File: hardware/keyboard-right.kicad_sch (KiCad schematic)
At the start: 84 parts, among them J1 BATT, J2 nice!view, J4 NUM_PAD, SW1 ON/OFF, SW10 U, SW11 I, SW12 O, SW13 P, SW14 {, SW15 H, SW16 J, SW17 K, SW18 L, SW19 ;, SW2 NRST, SW20 ', SW21 __ENTER, SW22 N, SW23 M, SW24 ,, SW25 ., SW26 /, SW27 SHIFT, SW28 UP, SW29 M1, SW3 6, SW30 DOWN, SW31 LEFT, SW32 ALT_2, SW33 RIGHT, SW34 DEL, SW35 }, SW36 SPACE, SW4 7, SW5 8, SW6 9, SW7 0, SW8 -, SW9 Y, U1 nice!nano

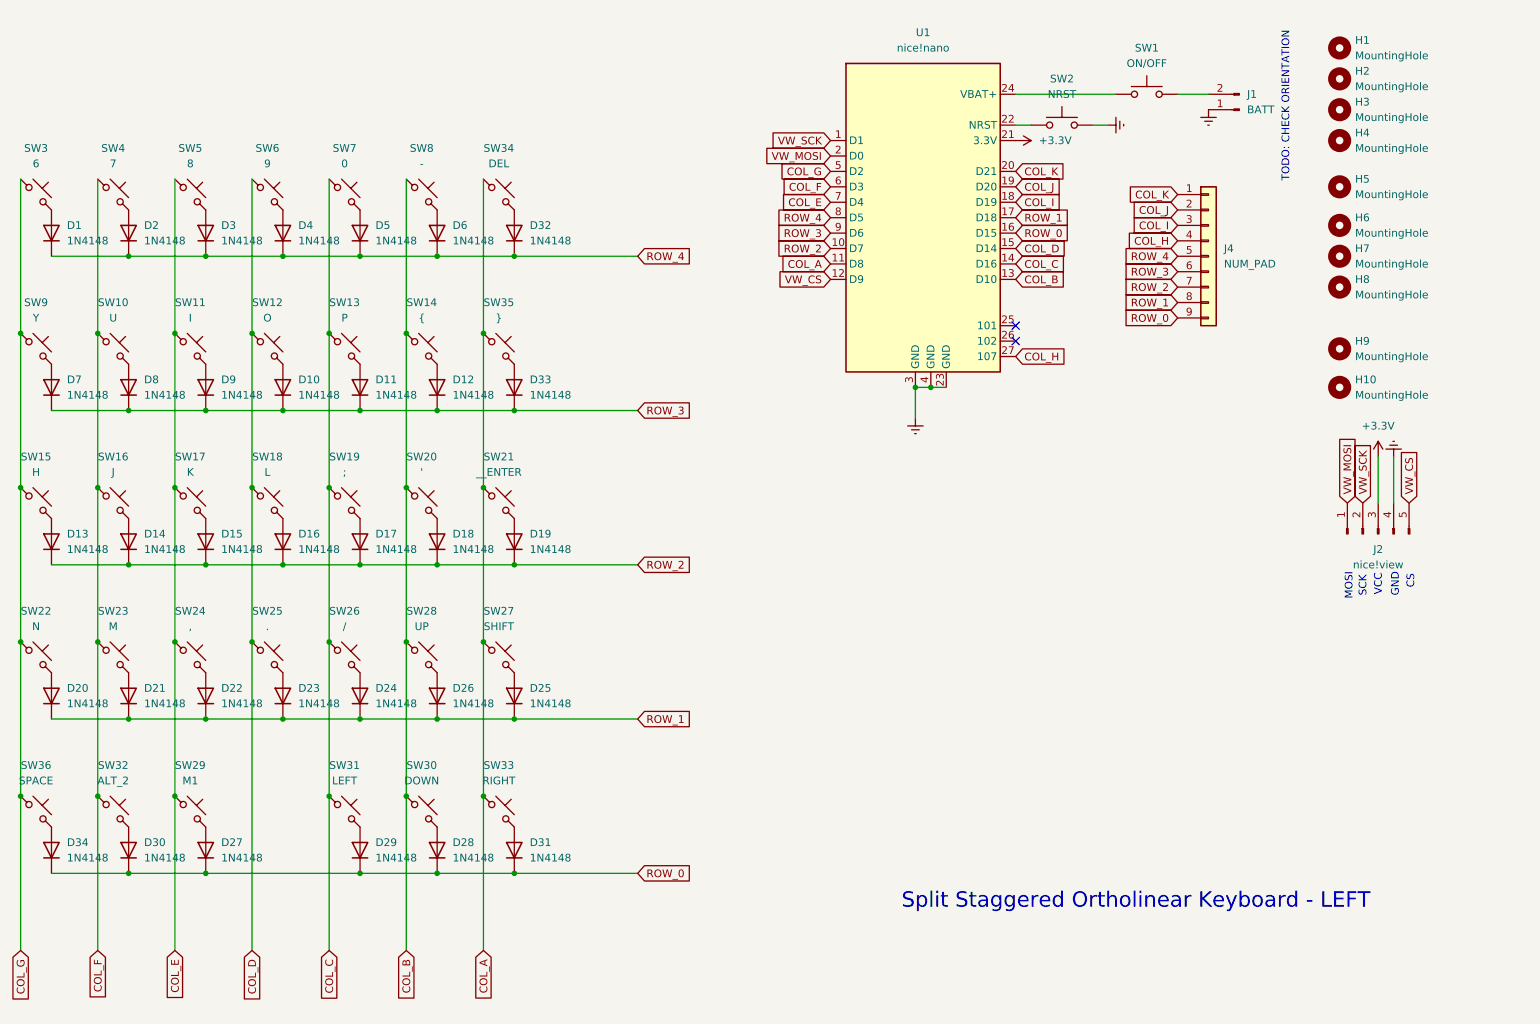
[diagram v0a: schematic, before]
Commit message: finish right keyboard, generate 3D models, add distribution folders
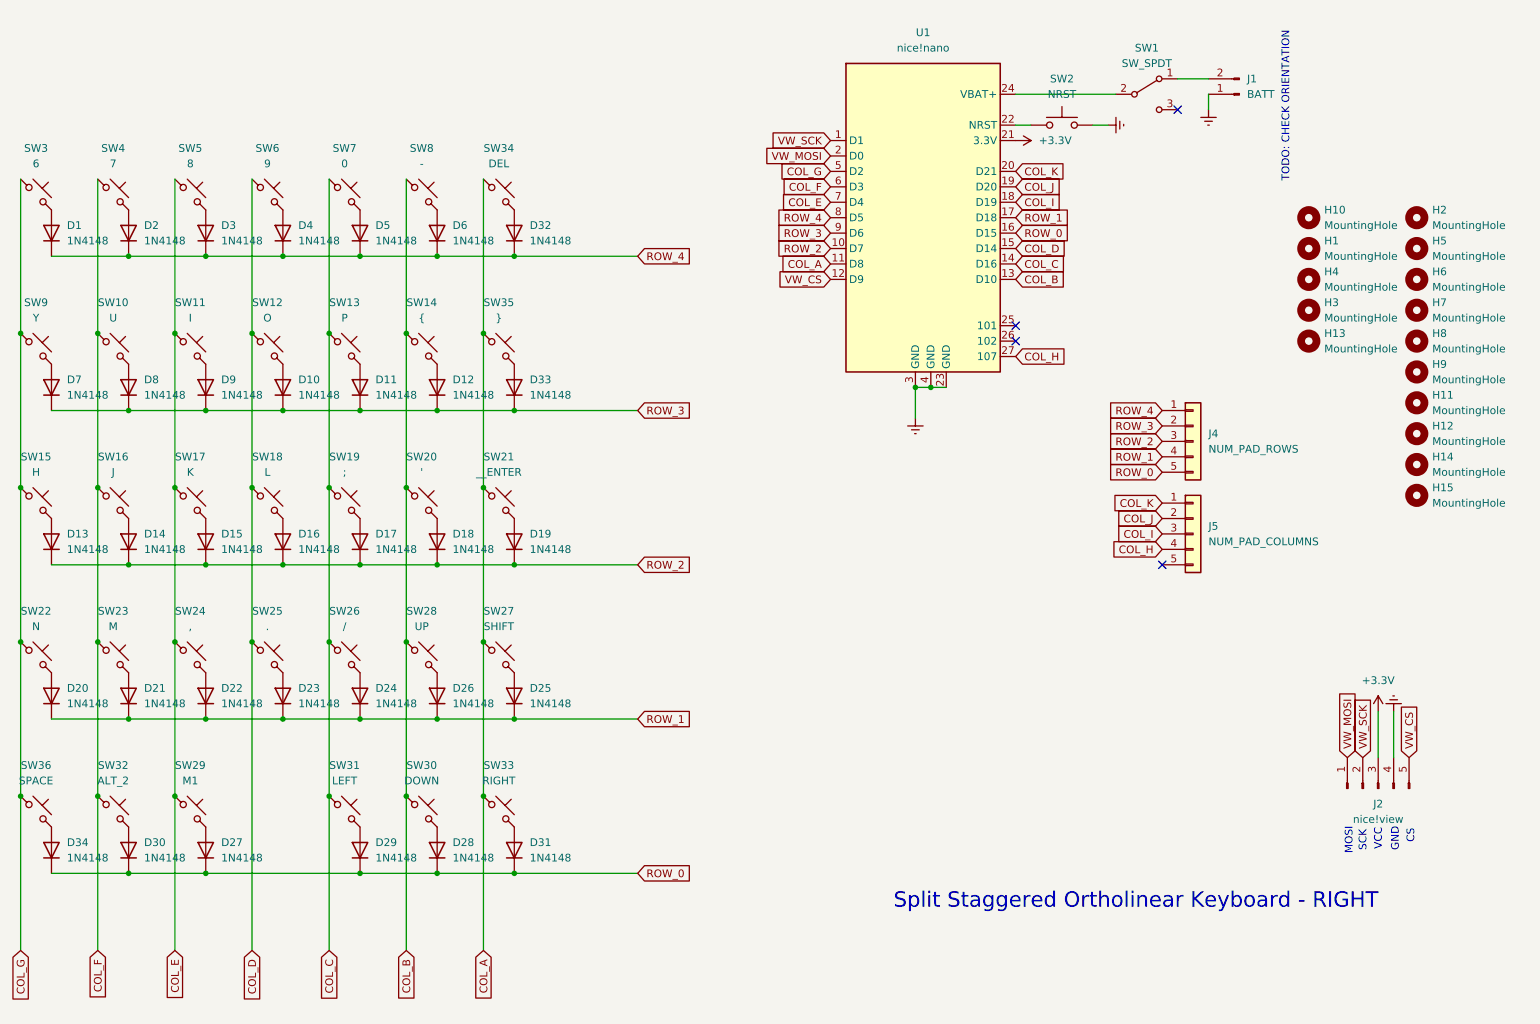
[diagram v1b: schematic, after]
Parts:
- removed J4: NUM_PAD, symbol Connector_Generic:Conn_01x09
- removed SW1: ON/OFF, Button_Switch_THT:SW_Slide_SPDT_Angled_CK_OS102011MA1Q, symbol Switch:SW_Push
- added H11, H12, H14, H15: MountingHole, keyboard:MountingPin_M2, symbol Mechanical:MountingHole
- added H13: MountingHole, keyboard:MountingPin_M3, symbol Mechanical:MountingHole
- added J4: NUM_PAD_ROWS, Connector_PinHeader_2.54mm:PinHeader_1x05_P2.54mm_Horizontal, symbol Connector_Generic:Conn_01x05
- added J5: NUM_PAD_COLUMNS, Connector_PinHeader_2.54mm:PinHeader_1x05_P2.54mm_Horizontal, symbol Connector_Generic:Conn_01x05
- added SW1: SW_SPDT, ScottoKeebs_Components:Switch_MSK12C02, symbol synth:SW_SPDT
- H1, H10, H3, H4: footprint MountingHole:MountingHole_3.2mm_M3 -> keyboard:MountingPin_M3
- H2, H5, H6, H7, H8, H9: footprint MountingHole:MountingHole_2.2mm_M2 -> keyboard:MountingPin_M2
- J1: footprint Connector_JST:JST_ZH_B2B-ZR_1x02_P1.50mm_Vertical -> Connector_JST:JST_PH_S2B-PH-K_1x02_P2.00mm_Horizontal
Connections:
- net COL_H: now also J5.4 (Pin_4)
- net COL_I: now also J5.3 (Pin_3)
- net COL_J: now also J5.2 (Pin_2)
- net COL_K: now also J5.1 (Pin_1)
- net ROW_0: now also J4.5 (Pin_5)
- net ROW_1: now also J4.4 (Pin_4)
- net ROW_2: now also J4.3 (Pin_3)
- net ROW_3: now also J4.2 (Pin_2)
- net ROW_4: now also J4.1 (Pin_1)
- net at J1.2 (Pin_2): now also SW1.1 (A)
- net at U1.24 (VBAT+): now also SW1.2 (B)
- no-connect marks 2 -> 4
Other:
- note added: "Split Staggered Ortholinear Keyboard - RIGHT"
- note removed: "Split Staggered Ortholinear Keyboard - LEFT"
- moved on the sheet: H1, H10, H2, H3, H4, H5, H6, H7, H8, H9, J1, J2
